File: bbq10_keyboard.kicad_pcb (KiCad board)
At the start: 2 copper layers, 68 x 45 mm, 20 parts, among them J1 PMOD, Q1 BSS138, U1 BBQ10KBD, U2 ATSAMD20E16A

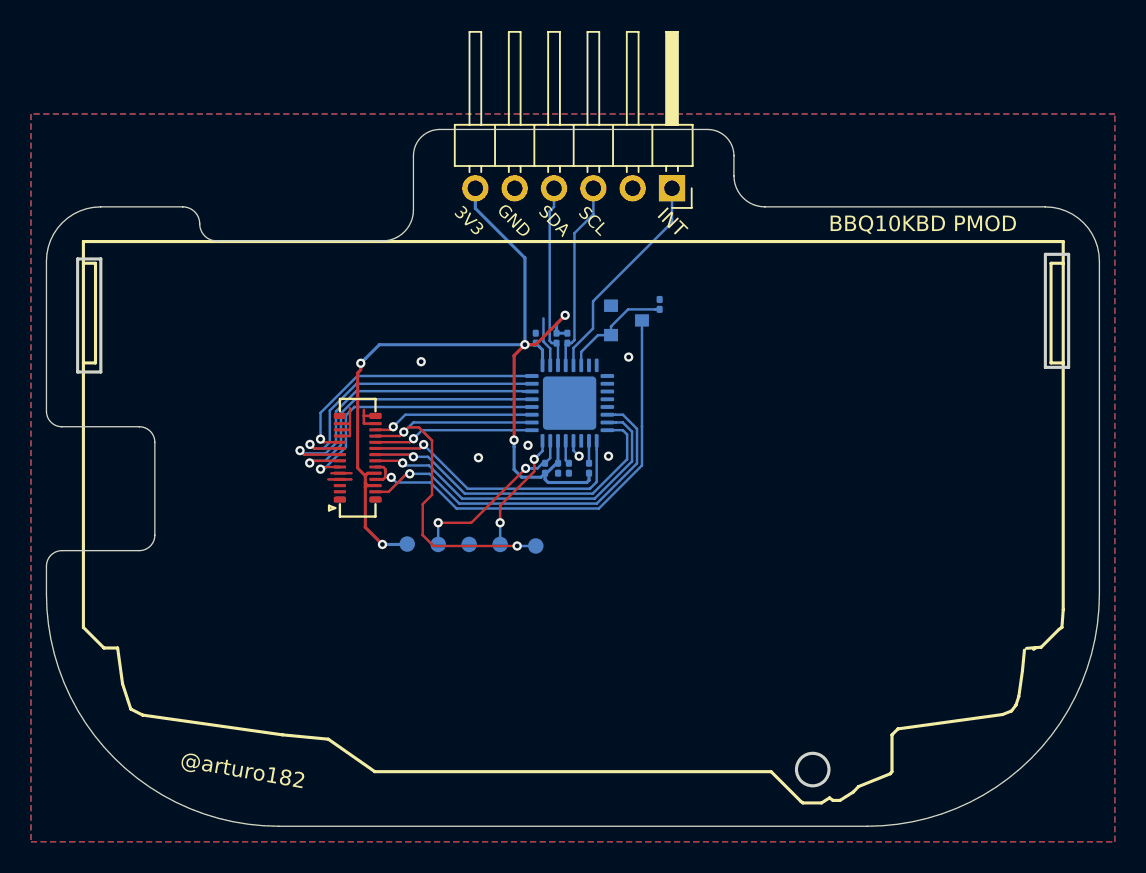
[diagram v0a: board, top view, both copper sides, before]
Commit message: rev2
- Made the right keyboard hole larger
- Moved the conenctor to the back
- Rerouted everything
- Fixed the damn 0201 footprints
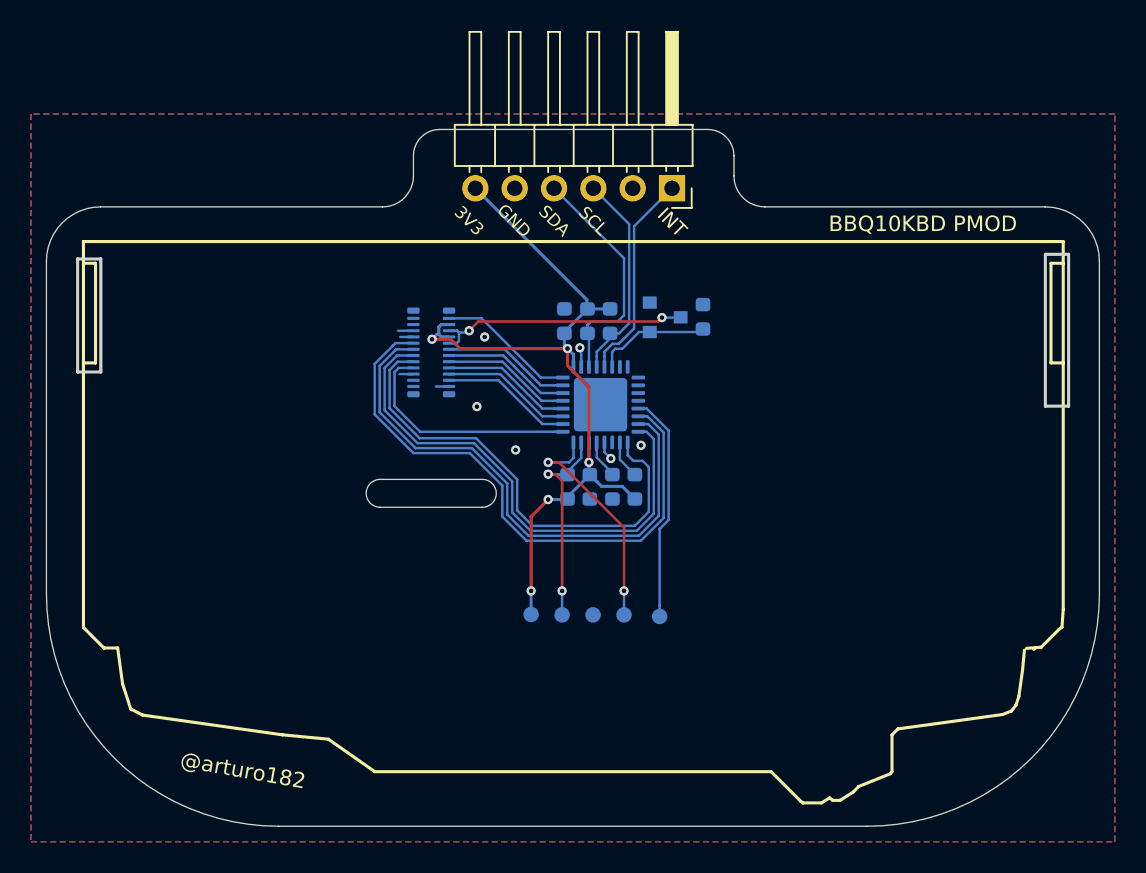
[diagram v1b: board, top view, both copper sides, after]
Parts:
- C1, C2, C3: footprint Capacitor_SMD:C_0201_0603Metric -> Capacitor_SMD:C_0603_1608Metric
- R1, R2, R3, R4, R5: footprint Resistor_SMD:R_0201_0603Metric -> Resistor_SMD:R_0603_1608Metric
- U1: moved to B.Cu
- moved TP4 9.20 mm to (145.3, 108.3)
- moved TP1 9.20 mm to (147.3, 108.3)
- moved TP2 9.20 mm to (151.3, 108.3)
- moved TP3 9.20 mm to (153.6, 108.5)
- moved TP5 9.20 mm to (149.3, 108.3)
- moved U1 8.29 mm to (138.8, 91.4), turned to 270 degrees
- moved R3 3.19 mm to (152.0, 100.1)
- moved C3 3.05 mm to (150.6, 100.1)
- moved R5 2.97 mm to (150.4, 89.4)
- moved R1 2.91 mm to (156.4, 89.1)
- moved Q1 2.51 mm to (154.0, 89.1)
- moved C1 2.38 mm to (149.1, 100.1)
- moved R4 2.28 mm to (148.9, 89.4)
- moved C2 2.15 mm to (147.4, 89.4)
- moved U2 2.00 mm to (149.8, 94.8)
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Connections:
- TP3 pad 1: /ROW3 -> /UART_TX
- U2 pad 1: /COL5 -> /COL3
- U2 pad 2: /ROW3 -> /COL4
- U2 pad 21: Net-(U2-Pad21) -> /UART_TX
- U2 pad 22: /ROW7 -> /ROW1
- U2 pad 23: /ROW6 -> /COL1
- U2 pad 24: /ROW5 -> /ROW2
- U2 pad 25: /ROW4 -> /COL2
- U2 pad 3: /COL4 -> /ROW3
- U2 pad 4: /ROW1 -> /COL5
- U2 pad 5: /COL1 -> /ROW4
- U2 pad 6: /ROW2 -> /ROW5
- U2 pad 7: /COL2 -> /ROW6
- U2 pad 8: /COL3 -> /ROW7
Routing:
- net /ROW1: track 17.8 -> 37.7 mm, vias 1 -> 0
- net /ROW3: track 26.7 -> 8.48 mm, vias 2 -> 0
- net /COL1: track 19.3 -> 35.5 mm, vias 1 -> 0
- net /ROW7: track 23.8 -> 8.93 mm, vias 1 -> 0
- net /UART_TX: track 0.00 -> 14.8 mm
- net /ROW6: track 22.3 -> 8.31 mm, vias 1 -> 0
- net Net-(Q1-Pad3): track 29.8 -> 16.7 mm, vias 1 -> 2
- net /ROW5: track 21.2 -> 8.35 mm, vias 1 -> 0
- net /ROW2: track 20.6 -> 33.2 mm, vias 1 -> 0
- net /COL2: track 19.4 -> 31.1 mm, vias 1 -> 0
- net +3V3: track 63.1 -> 53.1 mm
- net /ROW4: track 18.4 -> 8.39 mm, vias 1 -> 0
- net Net-(TP2-Pad1): track 7.82 -> 15.0 mm
- net GND: track 13.3 -> 6.08 mm
- net /SDA: track 11.9 -> 15.4 mm
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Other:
- outline, holes or cut-outs redrawn
- board text added: "BBQ10KBD PMOD rev2 Nov 2018 by @arturo182"
- board text removed: "BBQ10KBD PMOD rev1 Nov 2018 by @arturo182"
